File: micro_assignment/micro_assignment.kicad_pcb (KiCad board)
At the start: 2 copper layers, 69.1 x 77.1 mm, 39 parts, among them J1 Conn_01x06_Male, J2 USB_B_Micro, Q1 MURATA-FILTER_CSTCR, SW1 SW_Push, SW2 SW_Push, U1 AP7312, U11 SD-105162, U6 F552X---PN80, U7 ICM-20689, X1 MS3V-T1R

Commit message: Updated assignment and overhauled part of solution
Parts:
- removed C19: 470n, Capacitor_SMD:C_0805_2012Metric_Pad1.15x1.40mm_HandSolder
- removed C20: 2u2, Capacitor_SMD:C_0805_2012Metric_Pad1.15x1.40mm_HandSolder
- removed C21: 100n, Capacitor_SMD:C_0805_2012Metric_Pad1.15x1.40mm_HandSolder
- removed C22: 10n, Capacitor_SMD:C_0805_2012Metric_Pad1.15x1.40mm_HandSolder
- removed U11: SD-105162, micro:SD-105162
- removed U7: ICM-20689, Housings_DFN_QFN:QFN-24-1EP_4x4mm_Pitch0.5mm
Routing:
- net /MISO: track 130.4 -> 0.00 mm, vias 3 -> 0
- net /MOSI: track 127.2 -> 0.00 mm, vias 3 -> 0
- net /SCK: track 125.1 -> 0.00 mm, vias 3 -> 0
- net +3V3: track 211.6 -> 131.1 mm
- net /DET_SD: track 57.6 -> 3.11 mm, vias 2 -> 1
- net /CS_SD: track 74.7 -> 24.6 mm, vias 2 -> 1
- net /INT_ICM: track 37.7 -> 0.00 mm, vias 2 -> 0
- net /CS_ICM: track 32.8 -> 0.00 mm, vias 2 -> 0
- net GND: track 64.9 -> 49.0 mm, vias 79 -> 50
- net Net-(C19-Pad1): track 3.02 -> 0.00 mm

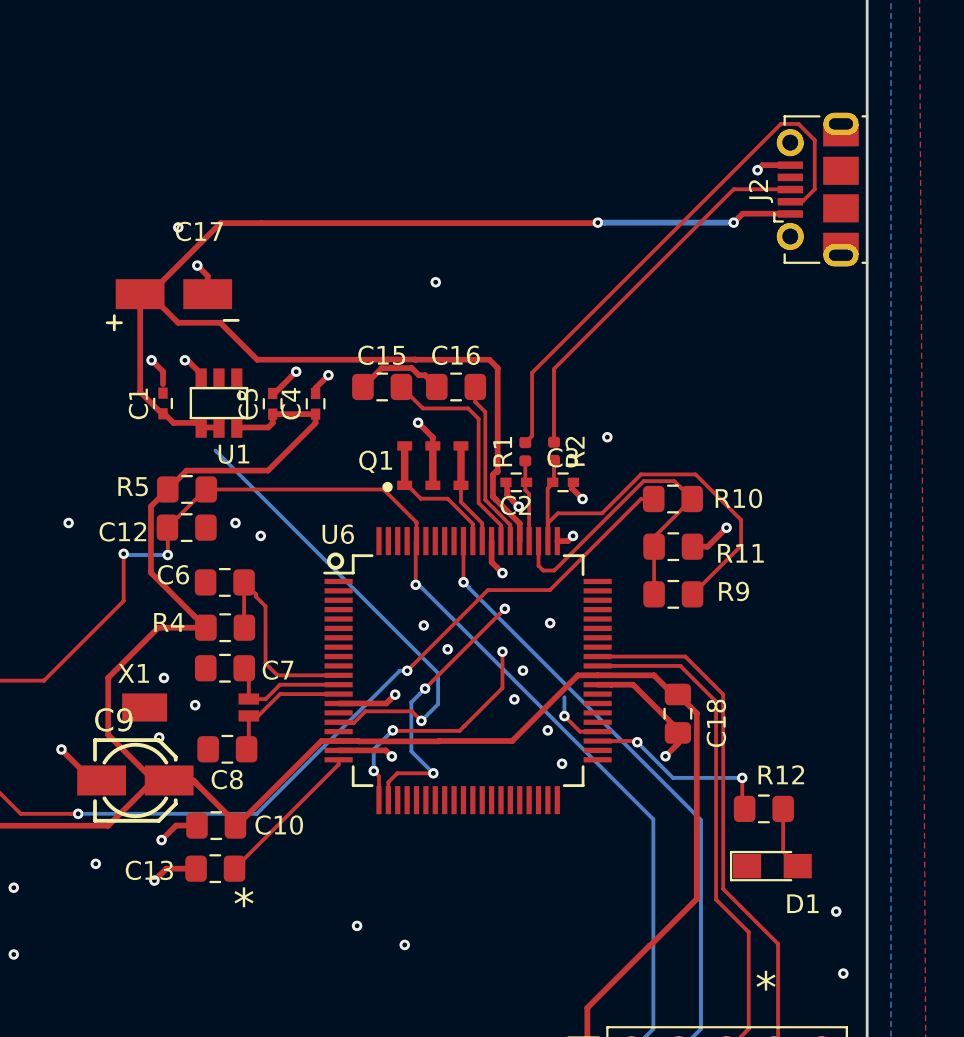
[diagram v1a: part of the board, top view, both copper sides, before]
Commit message: renaming micro and making the footprints assigned for assignment version of the layout
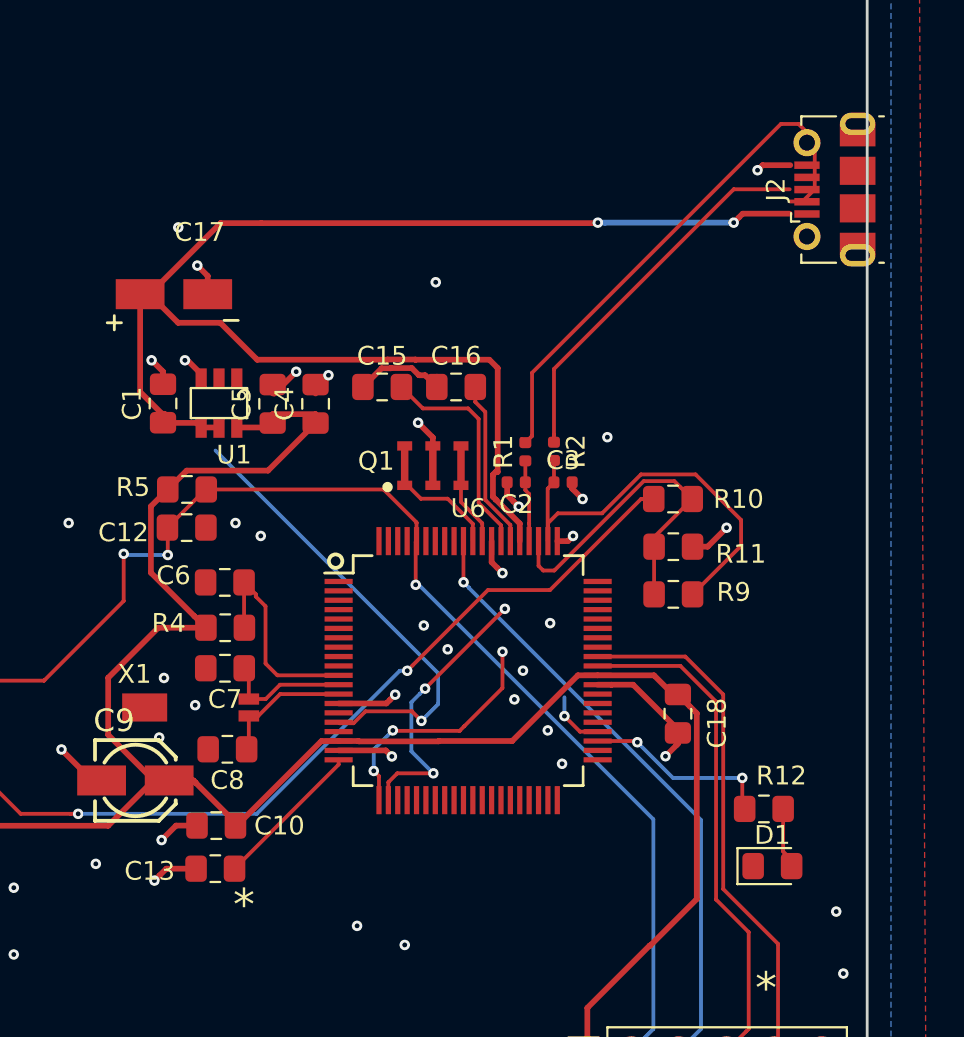
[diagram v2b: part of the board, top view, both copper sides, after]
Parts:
- C1, C4, C5: footprint Capacitors_SMD:C_0402 -> Capacitor_SMD:C_0805_2012Metric_Pad1.15x1.40mm_HandSolder
- C17: footprint v02:C_SMD_WURTH_865080540002 -> micro:C_SMD_WURTH_865080540002
- C2, C3: footprint Capacitors_SMD:C_0402 -> Capacitor_SMD:C_0402_1005Metric
- D1: footprint LEDs:LED_0805_HandSoldering -> LED_SMD:LED_0805_2012Metric_Pad1.15x1.40mm_HandSolder
- J1: footprint Pin_Headers:Pin_Header_Straight_1x06_Pitch2.54mm -> Connector_PinHeader_2.54mm:PinHeader_1x06_P2.54mm_Vertical
- J2: footprint Connectors_USB:USB_Micro-B_Molex-105017-0001 -> Connector_USB:USB_Micro-B_Molex-105017-0001
- SW1, SW2: footprint Buttons_Switches_THT:SW_PUSH_6mm -> Button_Switch_THT:SW_PUSH_6mm
- U6: footprint Housings_QFP:LQFP-80_12x12mm_Pitch0.5mm -> Package_QFP:LQFP-80_12x12mm_P0.5mm
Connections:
- X1 pad 1: Net-(C8-Pad1) -> Net-(X1-Pad1)
- X1 pad 2: Net-(C7-Pad1) -> Net-(X1-Pad2)

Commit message: Removed net labels from microcontroller assignment schematic
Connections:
- net /CS_ICM renamed Net-(U6-Pad8)
- net /CS_SD renamed Net-(U6-Pad16)
- net /DET_SD renamed Net-(U6-Pad44)
- net /INT_ICM renamed Net-(U6-Pad9)
- net /MISO renamed Net-(U6-Pad41)
- net /MOSI renamed Net-(U6-Pad40)
- net /SCK renamed Net-(U6-Pad36)
- net /SCL renamed Net-(U6-Pad38)
- net /SDA renamed Net-(U6-Pad37)
- net /STE renamed Net-(U6-Pad39)
